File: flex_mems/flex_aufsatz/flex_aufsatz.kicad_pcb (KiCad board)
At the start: 2 copper layers, 11 parts, among them IC1 ADPL44002AUJZ-1.8-R7, J1 Conn_01x22_Socket, J2 Conn_01x22_Socket, J3 10164228-0101A1RLF, J4 10164228-0101A1RLF, U1 ADAU7118ACPZRL

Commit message: flex_aufsatz1.0
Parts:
- moved IC1 89.7 mm to (102.0, 157.8)
- moved U1 82.8 mm to (114.2, 156.8), turned to 180 degrees
- moved C1 79.7 mm to (109.8, 157.3), turned to 90 degrees
- moved C2 79.1 mm to (117.8, 158.8)
- moved C3 77.8 mm to (98.4, 157.8)
- moved C6 70.4 mm to (105.5, 155.4), turned to -90 degrees
- moved J4 50.0 mm to (110.6, 113.9), turned to 90 degrees
- moved J3 50.0 mm to (106.5, 113.9), turned to 90 degrees
- moved J1 32.1 mm to (97.4, 100.2)
- moved J2 32.1 mm to (119.3, 100.0)
- moved C4 22.3 mm to (110.1, 105.6)
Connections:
- J1 pad 2: unconnected-(J1-Pin_2-Pad2) -> +3.3V
- J2 pad 21: unconnected-(J2-Pin_21-Pad21) -> GND
- J2 pad 22: unconnected-(J2-Pin_22-Pad22) -> GND
- J3 pad 1: +3V3 -> +3.3V
- J4 pad 1: +3V3 -> +3.3V
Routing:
- net +3.3V: track 0.00 -> 128.0 mm, vias 0 -> 6
- net GND: track 0.00 -> 124.5 mm, vias 0 -> 5
- net /WS: track 0.00 -> 54.7 mm
- net /MIC_CLK0: track 0.00 -> 53.3 mm, vias 0 -> 1
- net /BCLK: track 0.00 -> 53.0 mm
- net /MIC_DOUT_1: track 0.00 -> 50.4 mm, vias 0 -> 1
- net /MIC_DOUT_0: track 0.00 -> 50.2 mm, vias 0 -> 1
- net /MIC_DOUT_2: track 0.00 -> 49.2 mm, vias 0 -> 1
- net /MIC_CLK1: track 0.00 -> 48.2 mm, vias 0 -> 1
- net /TDM_DATA: track 0.00 -> 22.6 mm
- net +1V8: track 0.00 -> 22.6 mm
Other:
- board outline added: 27 x 62.6 mm

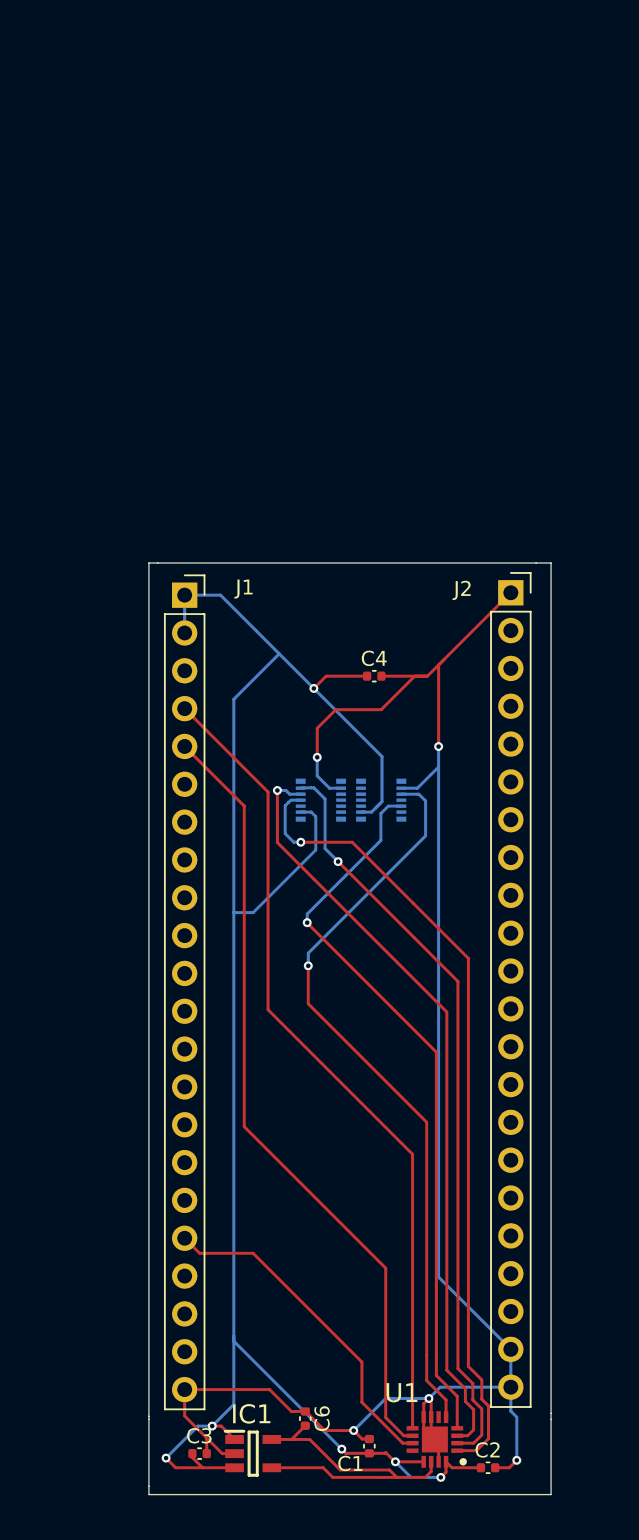
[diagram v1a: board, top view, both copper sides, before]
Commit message: GND zone update
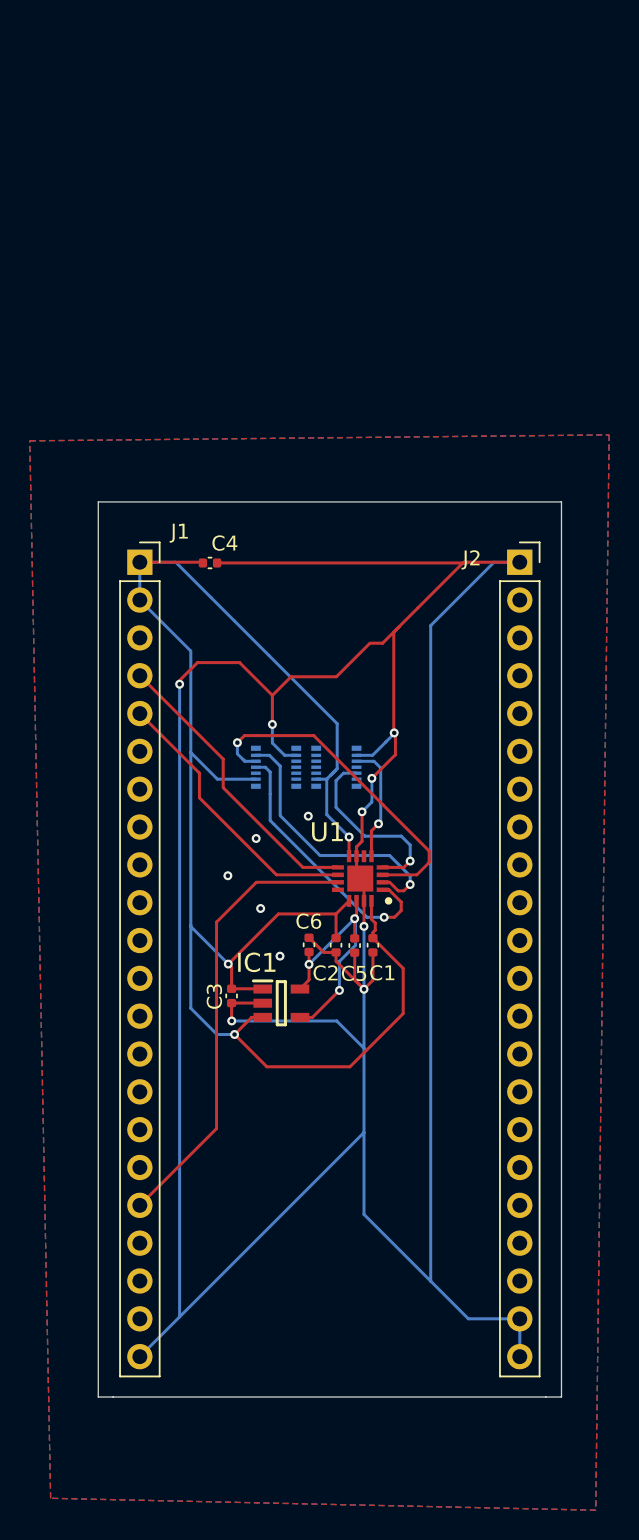
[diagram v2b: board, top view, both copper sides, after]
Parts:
- added C5: 100nF, Capacitor_SMD:C_0402_1005Metric, F.Cu at (108.8, 123.7)
- moved U1 38.0 mm to (109.2, 119.2)
- moved C2 36.5 mm to (107.6, 123.7), turned to -90 degrees
- moved C1 33.6 mm to (110.0, 123.7), turned to -90 degrees
- moved C6 31.8 mm to (105.8, 123.6)
- moved C3 30.8 mm to (100.5, 127.1), turned to -90 degrees
- moved IC1 30.3 mm to (103.9, 127.6)
- moved C4 13.4 mm to (99.1, 98.0)
- moved J1 3.73 mm to (94.4, 98.0)
- moved J3 3.73 mm to (103.5, 111.7)
- moved J4 3.73 mm to (107.6, 111.7)
- moved J2 2.14 mm to (119.9, 98.0)
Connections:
- U1 pad 8: GND -> +3.3V
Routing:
- net GND: track 124.5 -> 247.7 mm, vias 5 -> 13
- net /MIC_DOUT_2: track 49.2 -> 6.90 mm
- net /MIC_CLK1: track 48.2 -> 11.6 mm
- net /MIC_CLK0: track 53.3 -> 17.6 mm
- net /WS: track 54.7 -> 19.8 mm
- net /BCLK: track 53.0 -> 18.8 mm
- net /MIC_DOUT_0: track 50.2 -> 18.5 mm
- net /MIC_DOUT_1: track 50.4 -> 22.0 mm
- net +3.3V: track 128.0 -> 116.1 mm, vias 6 -> 3
- net /TDM_DATA: track 22.6 -> 30.4 mm
- net +1V8: track 22.6 -> 18.5 mm, vias 0 -> 3
- added copper zone on B.Cu, net GND
- added copper zone on F.Cu, net GND
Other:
- board size 27 x 62.6 mm -> 31.1 x 60.1 mm
